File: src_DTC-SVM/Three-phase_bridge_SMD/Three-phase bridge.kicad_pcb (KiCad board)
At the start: 2 copper layers, 419.1 x 318 mm, 101 parts, among them M1 MCP6022-I/P, M2 MCP6022-I/P, P1 CONN_1, P2 POWER_FUSE, P3 CONN_2, P4 CONN_1, P5 CONN_1, P6 POWER_FUSE, P7 CONN_1, P8 CONN_1, P9 CONN_1

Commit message: PCB: All resistances and most of capacitors have been replaced by their SMD counter parts. Required space have been sustancially reduced.
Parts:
- removed 1PIN (x8): P***, 1pin
- removed P7, P8, P9: CONN_1, PIN_ARRAY_1
- removed S6: IRF1010N, TO220_Big_Heat_Sink_Drain_Sink
- C10, C11, C18, C19, C20, C21, C8, C9: footprint 6mm_C -> c_1206
- D2, D3, D4: footprint LED-5MM -> LED-1206
- R1, R10, R11, R12, R13, R14, R15, R16, R17, R18, R19, R2, R20, R21, R22, R23, R24, R25, R26, R3, R4, R5, R6, R7, R8, R9: footprint R4 -> R_1206
- moved C1 114.9 mm to (82.8, 164.8)
- moved C18 104.0 mm to (413.8, 174.0)
- moved C19 104.0 mm to (403.6, 172.3)
- moved C20 104.0 mm to (416.3, 191.1)
- moved ACS1 104.0 mm to (401.8, 181.6)
- moved ACS2 104.0 mm to (402.0, 189.9)
- moved C21 104.0 mm to (416.4, 182.1)
- moved C3 100.4 mm to (111.0, 163.4)
- moved C4 87.8 mm to (66.2, 107.3)
- moved C2 87.8 mm to (65.9, 98.7)
- moved C8 84.8 mm to (82.2, 103.1), turned to 90 degrees
- moved P1 83.7 mm to (245.5, 37.1)
- moved R_Shunt_2 83.7 mm to (270.1, 69.1)
- moved C9 83.7 mm to (235.3, 26.2)
- moved C16 83.7 mm to (253.1, 23.6)
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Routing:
- net GND: track 929.4 -> 628.7 mm, vias 7 -> 3
- net VCC: track 333.5 -> 120.5 mm
- net +48V: track 422.0 -> 317.8 mm
- net N-0000056: track 151.9 -> 48.2 mm, vias 1 -> 0
- net N-0000019: track 129.8 -> 28.2 mm, vias 1 -> 0
- net (no net): track 0.00 -> 94.6 mm, vias 0 -> 1
- net +3.3V: track 103.9 -> 24.9 mm
- net N-0000037: track 96.5 -> 17.7 mm, vias 1 -> 0
- net N-0000025: track 153.0 -> 75.7 mm, vias 1 -> 0
- net N-0000021: track 125.4 -> 50.3 mm, vias 1 -> 0
- net N-0000047: track 105.4 -> 30.6 mm, vias 2 -> 1
- net VDD: track 240.8 -> 168.1 mm, vias 1 -> 0
- net N-0000024: track 104.8 -> 43.5 mm
- net N-0000014: track 162.3 -> 106.4 mm, vias 1 -> 0
- net N-0000012: track 85.7 -> 35.0 mm
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- added copper zone on F.Cu, net N-000006
- added copper zone on F.Cu, net N-0000061
- added copper zone on F.Cu, net N-0000062
- removed copper zone on B.Cu, net GND
- removed copper zone on F.Cu, net N-000005
- removed copper zone on F.Cu, net N-0000051
- removed copper zone on F.Cu, net N-0000057
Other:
- outline, holes or cut-outs redrawn

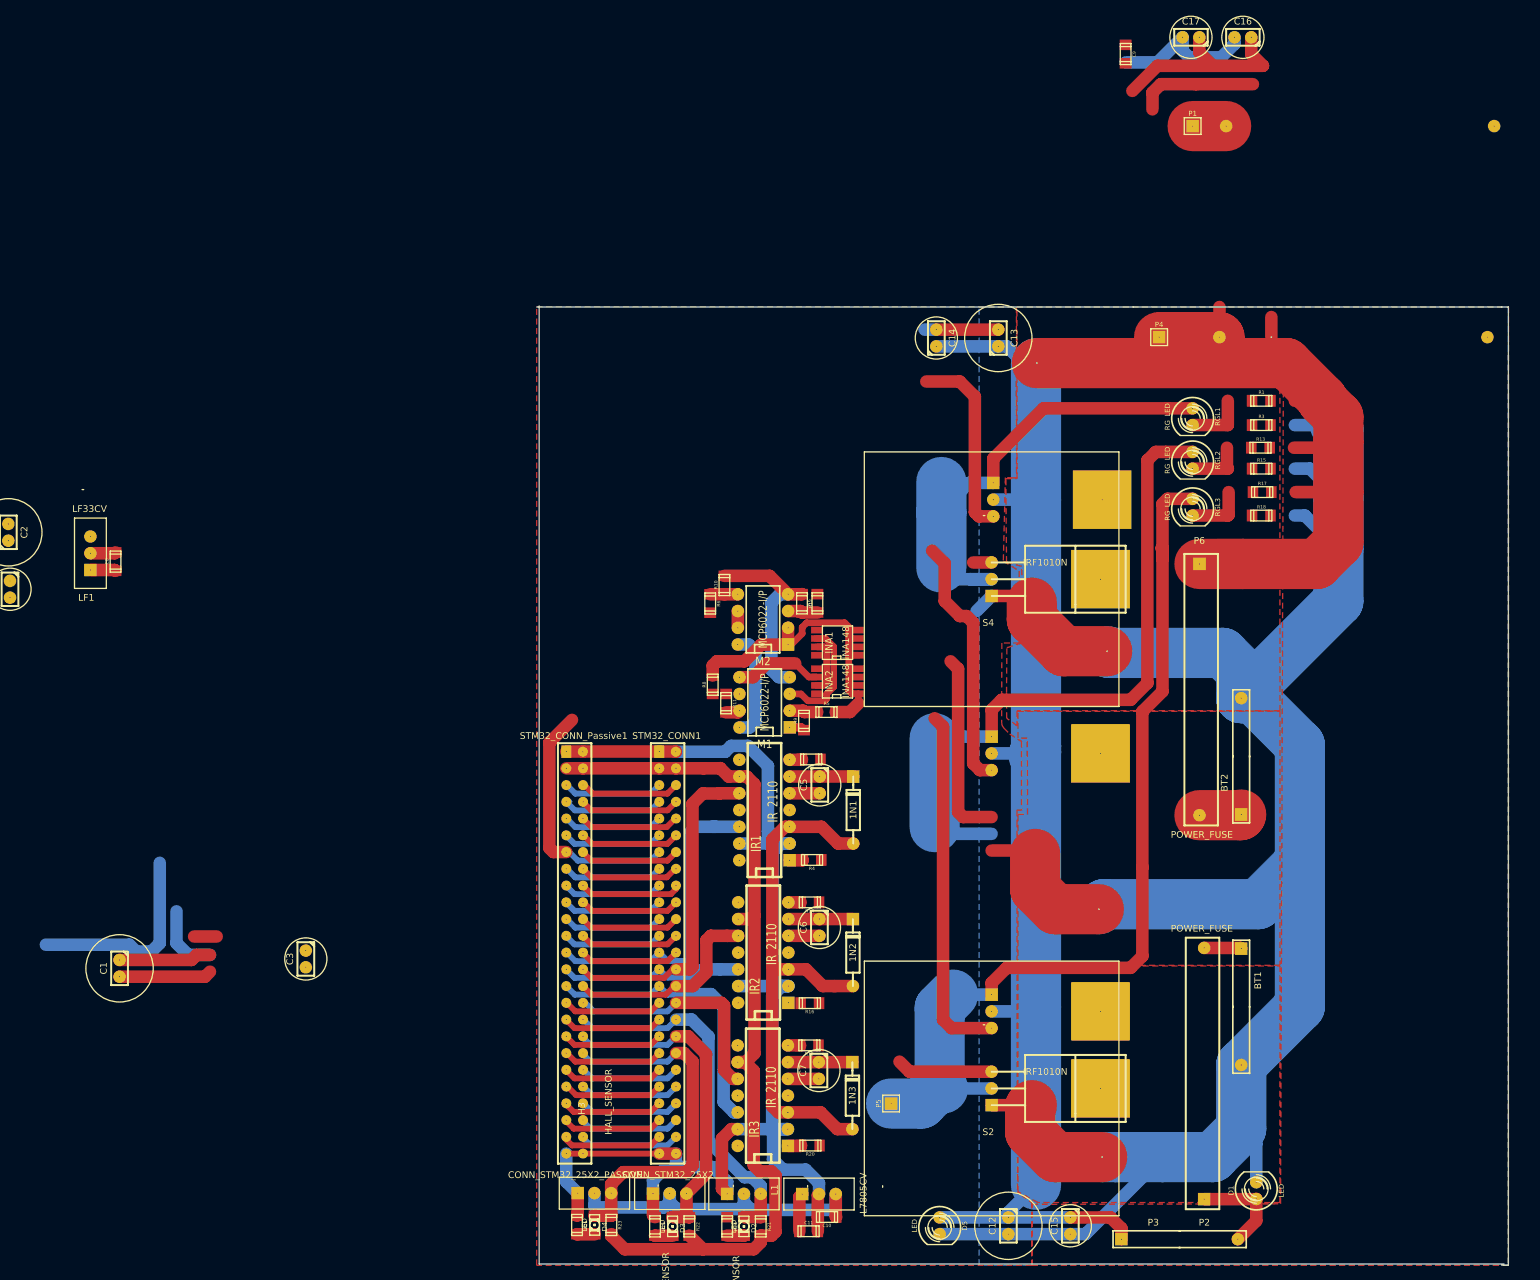
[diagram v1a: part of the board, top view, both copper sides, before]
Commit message: Most of the PCB has been compressed. Only the Red-green leds, fuses and diodes remains.
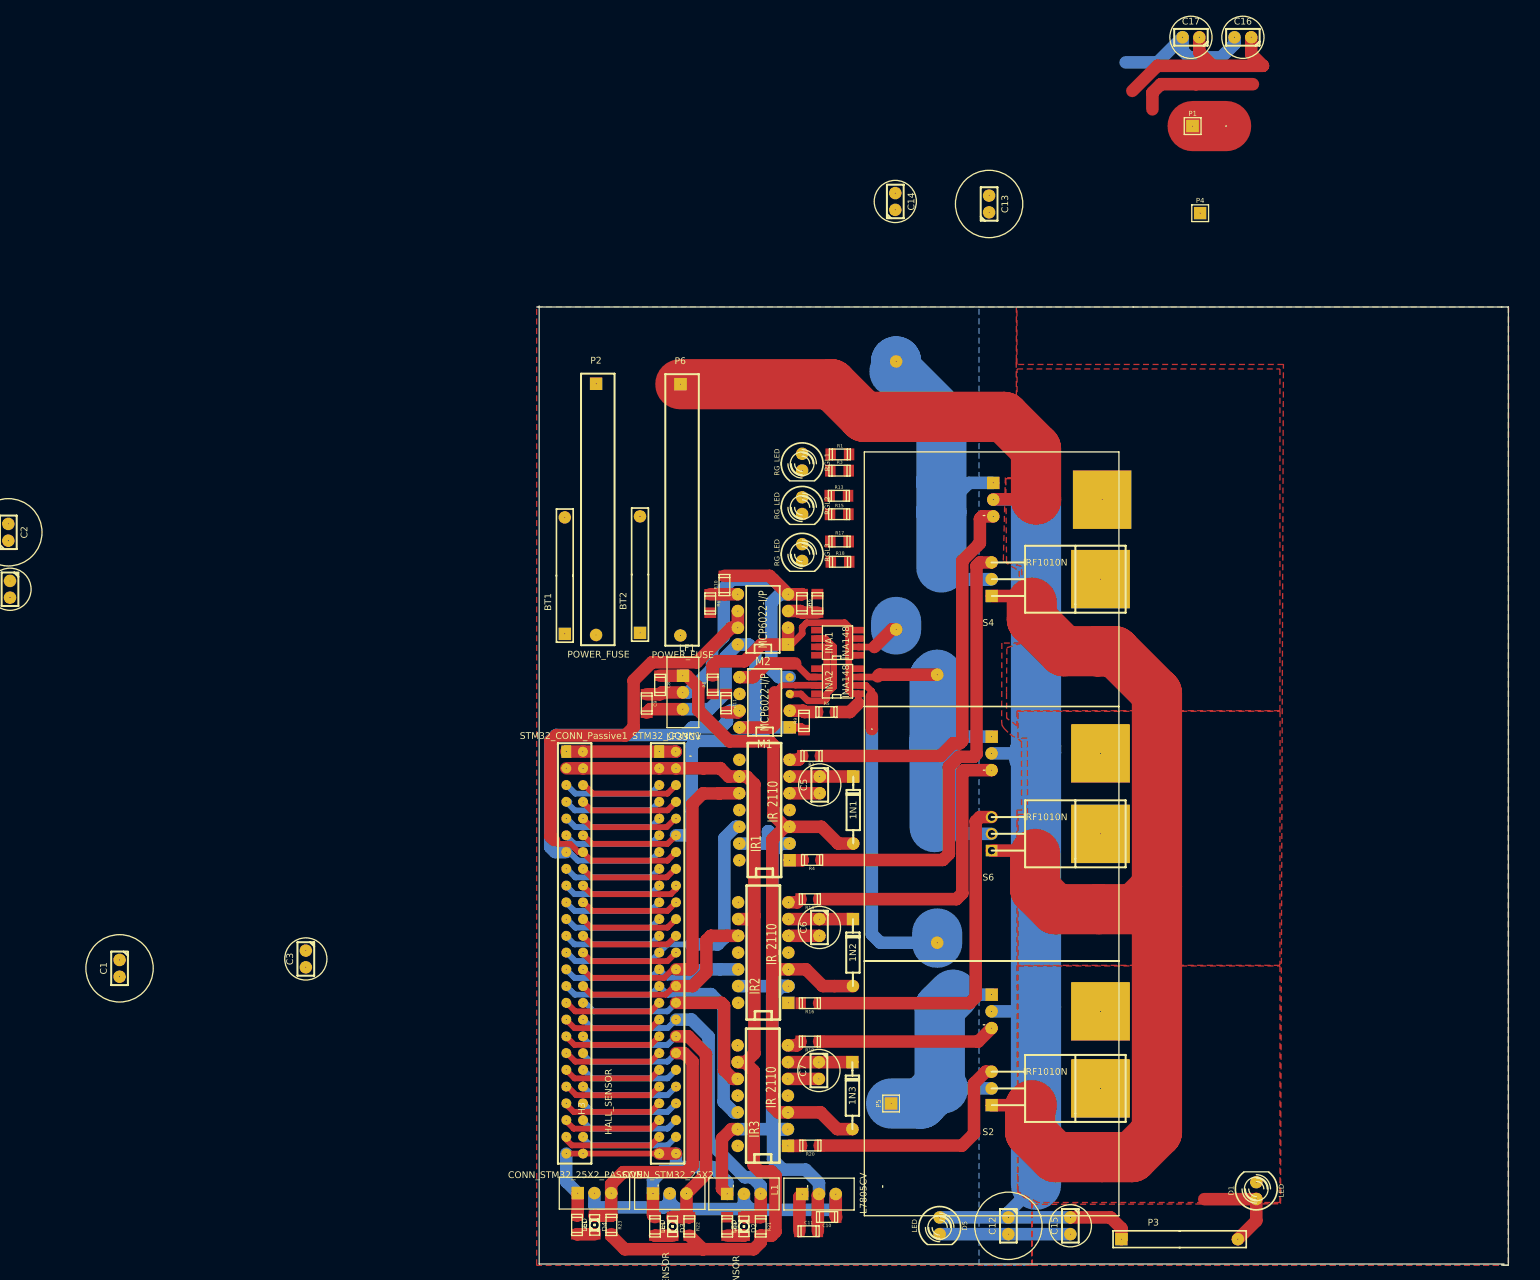
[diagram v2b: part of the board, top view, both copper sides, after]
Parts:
- added S6: IRF1010N, TO220_Big_Heat_Sink_Drain_Sink, F.Cu at (215.0, 144.4)
- moved BT1 122.4 mm to (150.3, 104.5), turned to 90 degrees
- moved C9 122.4 mm to (162.7, 124.6)
- moved P2 114.4 mm to (155.0, 104.1), turned to 0 degrees
- moved R_Shunt_2 95.4 mm to (206.8, 140.3), turned to 270 degrees
- moved BT2 95.2 mm to (161.7, 104.4)
- moved LF1 92.3 mm to (168.2, 123.0), turned to 180 degrees
- moved R_Shunt_1 90.0 mm to (200.5, 92.8), turned to 270 degrees
- moved C8 84.7 mm to (164.7, 121.8), turned to 270 degrees
- moved P6 83.3 mm to (167.8, 104.2)
- moved R17 64.5 mm to (191.9, 100.1)
- moved R1 64.4 mm to (192.0, 86.9)
- moved R15 64.4 mm to (191.9, 95.9)
- moved R13 64.3 mm to (191.8, 93.1)
- moved R3 64.3 mm to (191.9, 89.3)
- moved R18 64.3 mm to (192.0, 103.1)
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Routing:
- net GND: track 628.7 -> 450.4 mm, vias 3 -> 0
- net N-000007: track 140.0 -> 37.0 mm
- net +48V: track 317.8 -> 236.0 mm, vias 1 -> 0
- net (no net): track 94.6 -> 18.3 mm, vias 1 -> 0
- net N-0000092: track 2.79 -> 69.0 mm
- net N-0000037: track 17.7 -> 77.9 mm
- net N-0000082: track 0.00 -> 53.5 mm
- net N-0000014: track 106.4 -> 59.2 mm
- net +3.3V: track 24.9 -> 63.4 mm
- net N-0000069: track 17.5 -> 49.1 mm
- net N-0000090: track 28.9 -> 59.4 mm
- net N-0000035: track 22.4 -> 51.1 mm, vias 0 -> 1
- net N-0000098: track 54.1 -> 27.0 mm
- net N-0000033: track 41.0 -> 67.4 mm
- net N-0000097: track 14.6 -> 35.2 mm
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
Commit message: Changing leds to SMD.
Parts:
- RGL1, RGL2, RGL3: footprint LED-5MM -> LED_RG_1206
- moved R18 4.45 mm to (192.0, 98.7), turned to 180 degrees
- moved RGL3 4.21 mm to (186.9, 97.6), turned to 0 degrees
- moved R17 3.61 mm to (192.0, 96.5), turned to 180 degrees
- moved R15 1.92 mm to (192.1, 94.0), turned to 180 degrees
- moved RGL2 1.84 mm to (187.0, 92.9), turned to 0 degrees
- moved R13 1.30 mm to (192.1, 91.9), turned to 180 degrees
- moved RGL1 0.76 mm to (187.0, 88.2), turned to 0 degrees
- moved R1 0.28 mm to (192.1, 87.1), turned to 180 degrees
- moved R3 0.18 mm to (192.1, 89.3), turned to 180 degrees
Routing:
- net N-0000037: track 77.9 -> 23.0 mm
- net +48V: track 236.0 -> 185.1 mm
- net N-0000035: track 51.1 -> 1.40 mm, vias 1 -> 0
- net N-0000084: track 46.4 -> 2.54 mm
- net +3.3V: track 63.4 -> 37.9 mm
- net N-0000027: track 18.1 -> 0.47 mm
- net N-0000029: track 0.00 -> 11.1 mm
- net N-0000030: track 0.00 -> 10.8 mm
- net N-0000031: track 0.00 -> 10.7 mm
- net N-0000032: track 13.5 -> 4.19 mm
- net N-0000036: track 13.1 -> 6.22 mm
- net N-0000014: track 59.2 -> 63.6 mm
- net N-0000025: track 61.4 -> 65.8 mm
- net N-000007: track 37.0 -> 41.4 mm
- net N-000006: track 4.54 -> 2.34 mm
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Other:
- board size 419.1 x 318 mm -> 419.1 x 317.8 mm

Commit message: Before changing the fuses.
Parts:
- added R27: R, R_1206, F.Cu at (202.8, 205.0)
- added R28: R, R_1206, F.Cu at (161.6, 69.3)
- D1, D5: footprint LED-5MM -> LED-1206
- moved D1 163.3 mm to (155.5, 69.1), turned to 0 degrees
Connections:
- D1 pad 2: GND -> N-0000045
- D5 pad 2: GND -> N-0000044
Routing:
- added copper zone on F.Cu, net N-000006
- added copper zone on F.Cu, net N-0000061
- added copper zone on F.Cu, net N-0000062
- removed copper zone on F.Cu, net N-000002
- removed copper zone on F.Cu, net N-0000028
- removed copper zone on F.Cu, net N-0000063
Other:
- board size 419.1 x 317.8 mm -> 419.1 x 318 mm

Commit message: Fueses have been converted to SMD. THE ACS712/ACS714 have been wired.
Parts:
- ACS1, ACS2, C18, C19, C21: moved to B.Cu
- BT1, BT2: footprint Battery_2x1 -> PIN_ARRAY_2X1
- P2, P6: footprint Fuse -> fuse_holder_SMD
- moved C20 276.3 mm to (176.0, 54.7)
- moved C18 240.1 mm to (184.8, 101.7)
- moved C19 227.3 mm to (186.2, 105.9), turned to 90 degrees
- moved C21 226.1 mm to (191.0, 165.1), turned to 90 degrees
- moved ACS1 224.3 mm to (191.5, 103.6), turned to 270 degrees
- moved ACS2 207.3 mm to (196.5, 162.8), turned to 270 degrees
- moved P4 111.9 mm to (198.4, 151.3)
- moved P1 79.7 mm to (192.8, 96.9)
- moved R1 62.3 mm to (132.1, 70.7)
- moved R13 62.3 mm to (132.0, 75.5)
- moved R15 62.3 mm to (132.0, 77.6)
- moved R17 62.3 mm to (132.0, 80.1)
- moved R18 62.3 mm to (132.0, 82.3)
- moved R3 62.3 mm to (132.1, 72.9)
- moved RGL2 62.3 mm to (126.9, 76.6)
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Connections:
- ACS1 pad 1: N-0000019 (its old number) -> N-0000049
- ACS1 pad 2: N-0000019 (its old number) -> N-0000049
- ACS1 pad 3: N-0000051 (its old number) -> N-0000047
- ACS1 pad 4: N-0000051 (its old number) -> N-0000047
- ACS2 pad 1: N-0000011 (its old number) -> N-0000023
- ACS2 pad 2: N-0000011 (its old number) -> N-0000023
- ACS2 pad 3: N-0000032 (its old number) -> N-0000026
- ACS2 pad 4: N-0000032 (its old number) -> N-0000026
- INA1 pad 2: N-0000051 (its old number) -> N-0000047
- INA1 pad 3: N-0000019 (its old number) -> N-0000012
- INA2 pad 2: N-0000032 (its old number) -> N-0000026
- INA2 pad 3: N-0000011 (its old number) -> N-0000027
- P1 pad 1: N-0000051 (its old number) -> N-0000049
- P4 pad 1: N-0000032 (its old number) -> N-0000023
- RGL1 pad 1: N-0000019 (its old number) -> N-0000012
- RGL2 pad 1: N-0000011 (its old number) -> N-0000027
- R_Shunt_1 pad 1: N-0000019 (its old number) -> N-0000012
- R_Shunt_1 pad 2: N-0000051 (its old number) -> N-0000047
- R_Shunt_2 pad 1: N-0000011 (its old number) -> N-0000027
- R_Shunt_2 pad 2: N-0000032 (its old number) -> N-0000026
- S1 pad 1: N-0000019 (its old number) -> N-0000012
- S3 pad 1: N-0000011 (its old number) -> N-0000027
- S4 pad 3: N-0000019 (its old number) -> N-0000012
- S6 pad 3: N-0000011 (its old number) -> N-0000027
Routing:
- net +5V: track 50.3 -> 158.5 mm
- net N-0000012: track 0.00 -> 103.8 mm
- net N-0000019 (its old number): track 65.8 -> 0.00 mm
- net N-0000027: track 0.00 -> 64.7 mm
- net N-0000011 (its old number): track 63.6 -> 0.00 mm
- net N-0000034: track 67.4 -> 120.5 mm, vias 0 -> 1
- net GND: track 452.1 -> 489.9 mm
- net N-0000065: track 49.1 -> 80.3 mm
- net N-0000047: track 0.00 -> 28.0 mm
- net N-0000023: track 0.00 -> 21.8 mm
- net +3.3V: track 37.9 -> 59.3 mm
- net N-0000026: track 0.00 -> 18.3 mm
- net N-0000024: track 0.47 -> 18.6 mm
- net N-0000088: track 2.54 -> 15.1 mm
- net N-0000033: track 4.19 -> 13.5 mm
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- added copper zone on F.Cu, net N-000006
- added copper zone on F.Cu, net N-0000061
- added copper zone on F.Cu, net N-0000062
- removed copper zone on F.Cu, net N-0000037
- removed copper zone on F.Cu, net N-0000064
- removed copper zone on F.Cu, net N-000007
